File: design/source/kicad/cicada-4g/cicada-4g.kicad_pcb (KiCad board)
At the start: 4 copper layers, 40 x 65 mm, 87 parts, among them J2 Host, J3 USB_OTG, J4 IPX, J5 IPX, J6 IPX, J7 Conn_01x04, J8 IPX, P1 SK-C793, Q1 NMOS, Q2 NMOS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

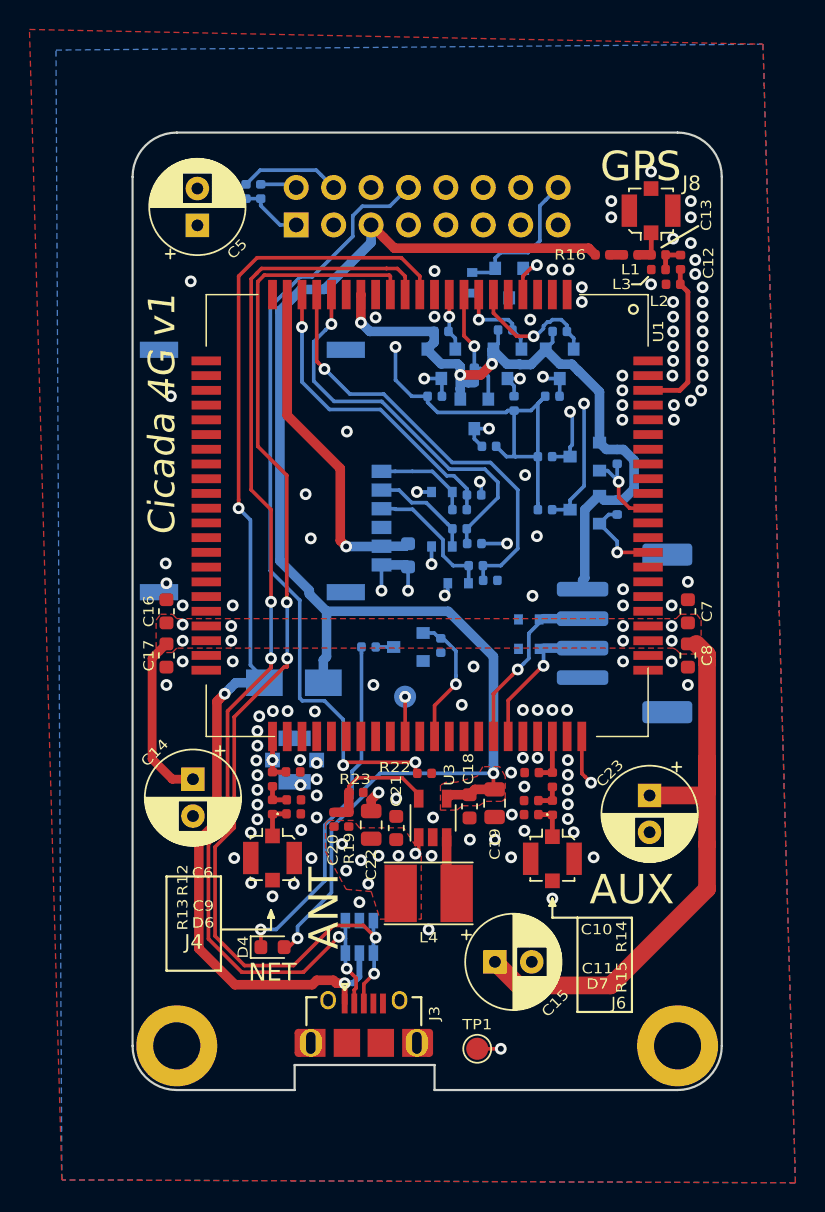
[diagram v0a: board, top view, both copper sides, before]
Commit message: Cicada 4G v1.1 - don't swap RX-TX
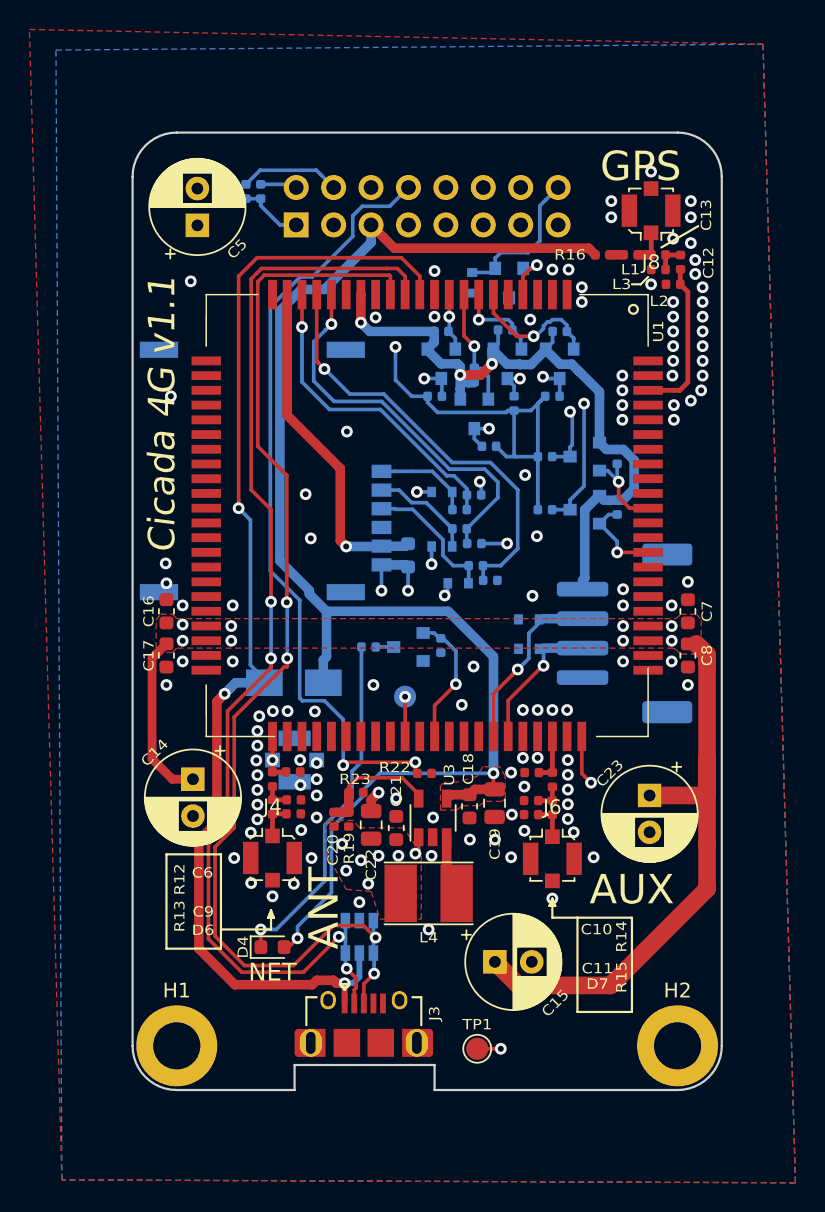
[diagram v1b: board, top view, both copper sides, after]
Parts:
- C13: value 33pF -> 33pF C0G
- J4, J5, J6, J8: footprint cicada-footprints:U.FL_Molex_MCRF_73412-0110_Vertical -> Connector_Coaxial:U.FL_Molex_MCRF_73412-0110_Vertical
- R10: value 220R -> 470R
- R17, R18, R20, R21, R24, R25, R26, R27, R3, R4, R5, R6: value 10k -> 4.7k
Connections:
- Q2 pad 3: /UART_RX_3v3 -> /UART_TX_3v3
- Q4 pad 3: /UART_TX_3v3 -> /UART_RX_3v3
- R4 pad 2: /UART_TX_3v3 -> /UART_RX_3v3
- R6 pad 2: /UART_RX_3v3 -> /UART_TX_3v3
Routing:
- net /UART_RX_3v3: track 22.6 -> 29.8 mm
- net /UART_TX_3v3: track 22.7 -> 19.1 mm
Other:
- board text added: "Cicada 4G v1.1"
- board text removed: "Cicada 4G v1"

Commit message: Update component library references in Cicada 4G
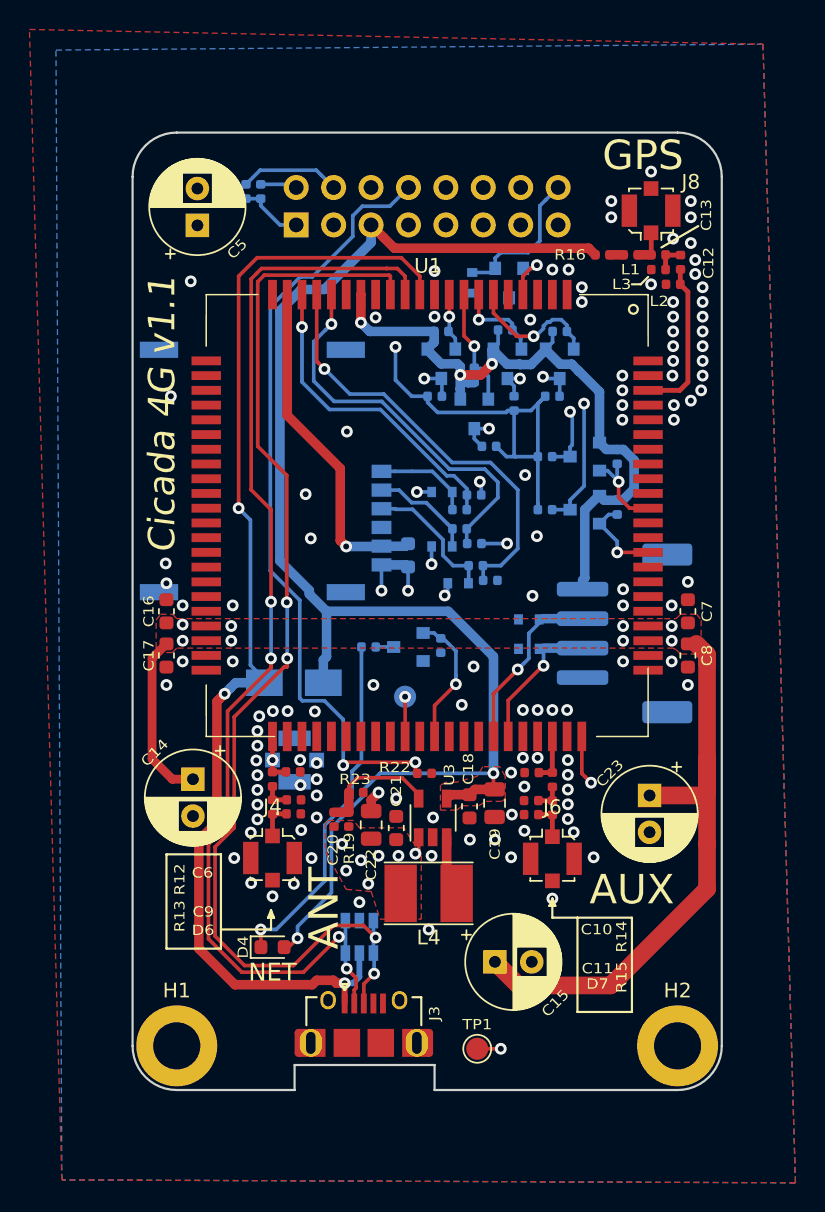
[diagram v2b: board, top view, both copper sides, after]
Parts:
- L4: footprint Inductor_SMD:L_Taiyo-Yuden_NR-40xx_HandSoldering -> cicada-footprints:L_4030_Handsoldering
- P1: footprint sk-c793:SK-C793 -> cicada-footprints:SK-C793
- U1: value sim7600 -> VAL**; footprint sim7600:sim7600 -> cicada-footprints:sim7600
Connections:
- H1 pad 1: Net-(H1-Pad1) -> (no net)
- H2 pad 1: Net-(H2-Pad1) -> (no net)
- J2 pad 14: /nCS_WIFI -> (no net)
- J3 pad 4: Net-(J3-Pad4) -> (no net)
- P1 pad 6: Net-(P1-Pad6) -> (no net)
- U1 pad 16: Net-(U1-Pad16) -> (no net)
- U1 pad 21: Net-(U1-Pad21) -> (no net)
- U1 pad 22: Net-(U1-Pad22) -> (no net)
- U1 pad 23: Net-(U1-Pad23) -> (no net)
- U1 pad 24: Net-(U1-Pad24) -> (no net)
- U1 pad 25: Net-(U1-Pad25) -> (no net)
- U1 pad 26: Net-(U1-Pad26) -> (no net)
- U1 pad 27: Net-(U1-Pad27) -> (no net)
- U1 pad 28: Net-(U1-Pad28) -> (no net)
- U1 pad 29: Net-(U1-Pad29) -> (no net)
- U1 pad 30: Net-(U1-Pad30) -> (no net)
- U1 pad 31: Net-(U1-Pad31) -> (no net)
- U1 pad 32: Net-(U1-Pad32) -> (no net)
- U1 pad 33: Net-(U1-Pad33) -> (no net)
- U1 pad 34: Net-(U1-Pad34) -> (no net)
- U1 pad 35: Net-(U1-Pad35) -> (no net)
- U1 pad 36: Net-(U1-Pad36) -> (no net)
- U1 pad 42: Net-(U1-Pad42) -> (no net)
- U1 pad 44: Net-(U1-Pad44) -> (no net)
- U1 pad 45: Net-(U1-Pad45) -> (no net)
- U1 pad 46: Net-(U1-Pad46) -> (no net)
- U1 pad 47: Net-(U1-Pad47) -> (no net)
- U1 pad 48: Net-(U1-Pad48) -> (no net)
- U1 pad 50: Net-(U1-Pad50) -> (no net)
- U1 pad 52: Net-(U1-Pad52) -> (no net)
- U1 pad 53: Net-(U1-Pad53) -> (no net)
- U1 pad 54: Net-(U1-Pad54) -> (no net)
- U1 pad 66: Net-(U1-Pad66) -> (no net)
- U1 pad 67: Net-(U1-Pad67) -> (no net)
- U1 pad 69: Net-(U1-Pad69) -> (no net)
- U1 pad 70: Net-(U1-Pad70) -> (no net)
- U1 pad 72: Net-(U1-Pad72) -> (no net)
- U1 pad 73: Net-(U1-Pad73) -> (no net)
- U1 pad 74: Net-(U1-Pad74) -> (no net)
- U1 pad 75: Net-(U1-Pad75) -> (no net)
- U1 pad 76: Net-(U1-Pad76) -> (no net)
- U1 pad 83: Net-(U1-Pad83) -> (no net)
- U1 pad 84: Net-(U1-Pad84) -> (no net)
- U1 pad 86: Net-(U1-Pad86) -> (no net)
- U1 pad 87: Net-(U1-Pad87) -> (no net)

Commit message: Update the library directory structure to match other Okra projects
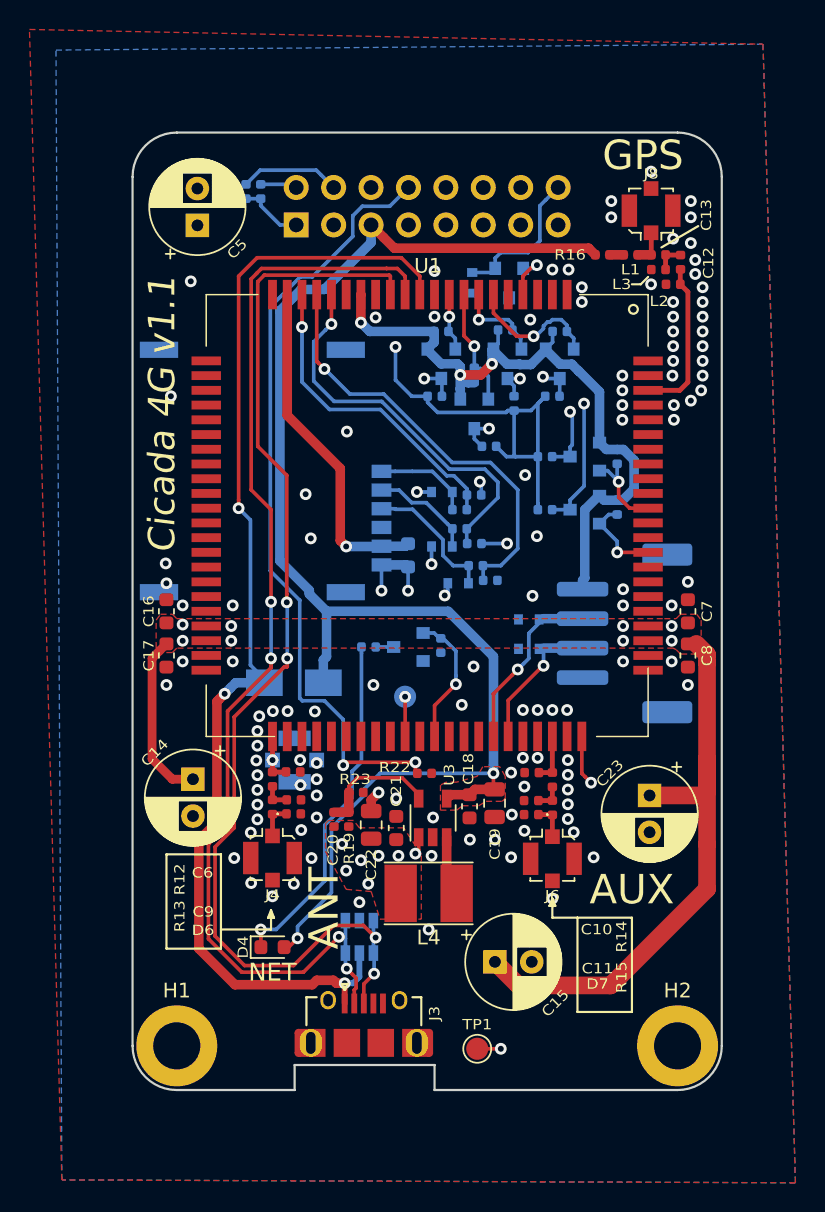
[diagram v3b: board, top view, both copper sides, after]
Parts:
- J4, J5, J6, J8: footprint Connector_Coaxial:U.FL_Molex_MCRF_73412-0110_Vertical -> cicada-footprints:U.FL_Molex_MCRF_73412-0110_Vertical
- U1: value VAL** -> sim7600
